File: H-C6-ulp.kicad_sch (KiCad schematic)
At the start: 76 parts, among them J1 USB_C_Receptacle_USB2.0, J2 AFC24-S24FIC-00, J3 SM02B-SRSS-TB(LF)(SN), J4 SM04B-SRSS-TB_LF__SN_, Q1 Si1308, Q2 Si2301CDS, SW1 SW_Push_Dual, SW2 SW_Push_Dual, U1 ESP32-C6, U2 SGM6029CYG/TR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

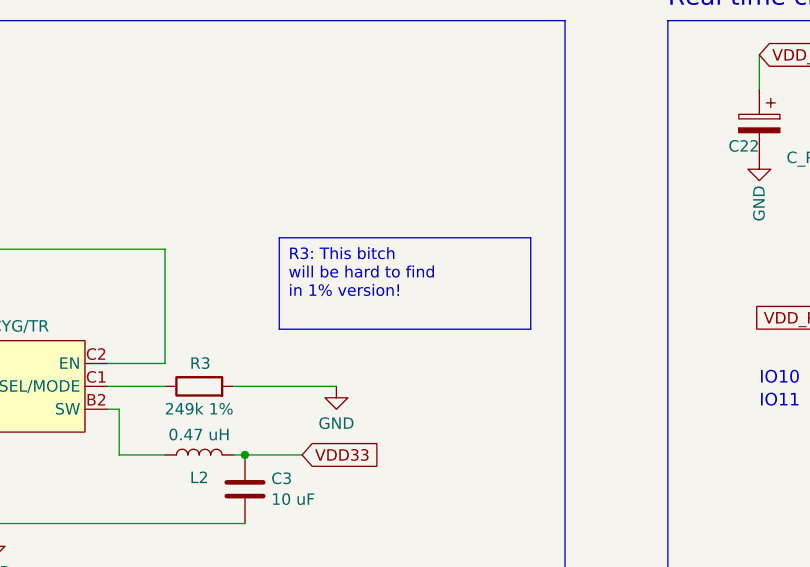
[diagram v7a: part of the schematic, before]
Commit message: Update L2 with same inductor 470nH than XIAO C6
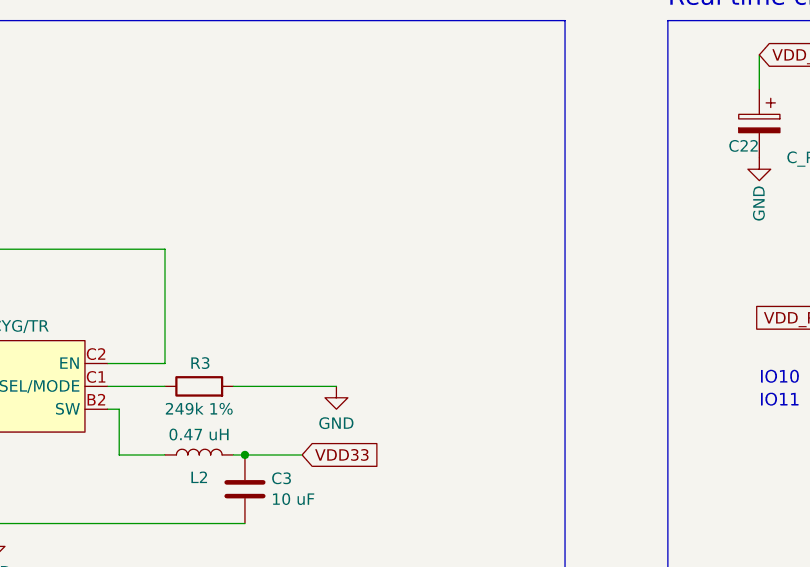
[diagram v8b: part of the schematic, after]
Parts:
- L2: footprint Inductor_SMD:L_0603_1608Metric -> footprints:IND-SMD_L2.5-W2.0_SPH252012; LCSC C5252358 -> C329586
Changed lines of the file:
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@@
     (fill (type none))
-  )
-  (text_box "R3: This bitch \n    will be hard to find\n    in 1% version!"
-    (at 148.59 224.79 0) (size 27.94 10.16)
-    (stroke (width 0) (type default) (color 194 0 0 1))
-    (fill (type none))
-    (effects (font (size 1.27 1.27) (color 194 0 0 1)) (justify left top))
   )
   (text "USB-C JTAG / CDC Serial to MCU" (at 115.57 129.54 0)
@@
       (effects (font (size 1.27 1.27)))
     )
-    (property "Footprint" "Inductor_SMD:L_0603_1608Metric" (at 139.7 248.92 0)
-      (effects (font (size 1.27 1.27)) hide)
-    )
-    (property "Datasheet" "https://jlcpcb.com/partdetail/ChilisinElec-BSCH001608082N7S00/C5252358" (at 139.7 248.92 0)
-      (effects (font (size 1.27 1.27)) hide)
-    )
-    (property "LCSC" "C5252358" (at 139.7 248.92 90)
-      (effects (font (size 1.27 1.27)) hide)
-    )
+    (property "Footprint" "footprints:IND-SMD_L2.5-W2.0_SPH252012" (at 139.7 248.92 0)
+      (effects (font (size 1.27 1.27)) hide)
+    )
+    (property "Datasheet" "https://jlcpcb.com/parts/2nd/Inductors_Coils_Chokes/Power_Inductors_81925" (at 139.7 248.92 0)
+      (effects (font (size 1.27 1.27)) hide)
+    )
+    (property "LCSC" "C329586" (at 139.7 248.92 90)
+      (effects (font (size 1.27 1.27)) hide)
+    )
